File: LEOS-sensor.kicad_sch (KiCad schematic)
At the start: 23 parts, among them J1 MicroFit_1x4, J2 MicroFit_1x4, U1 MCP2562FD, U2 MCP2518FD, Y1 40 MHz

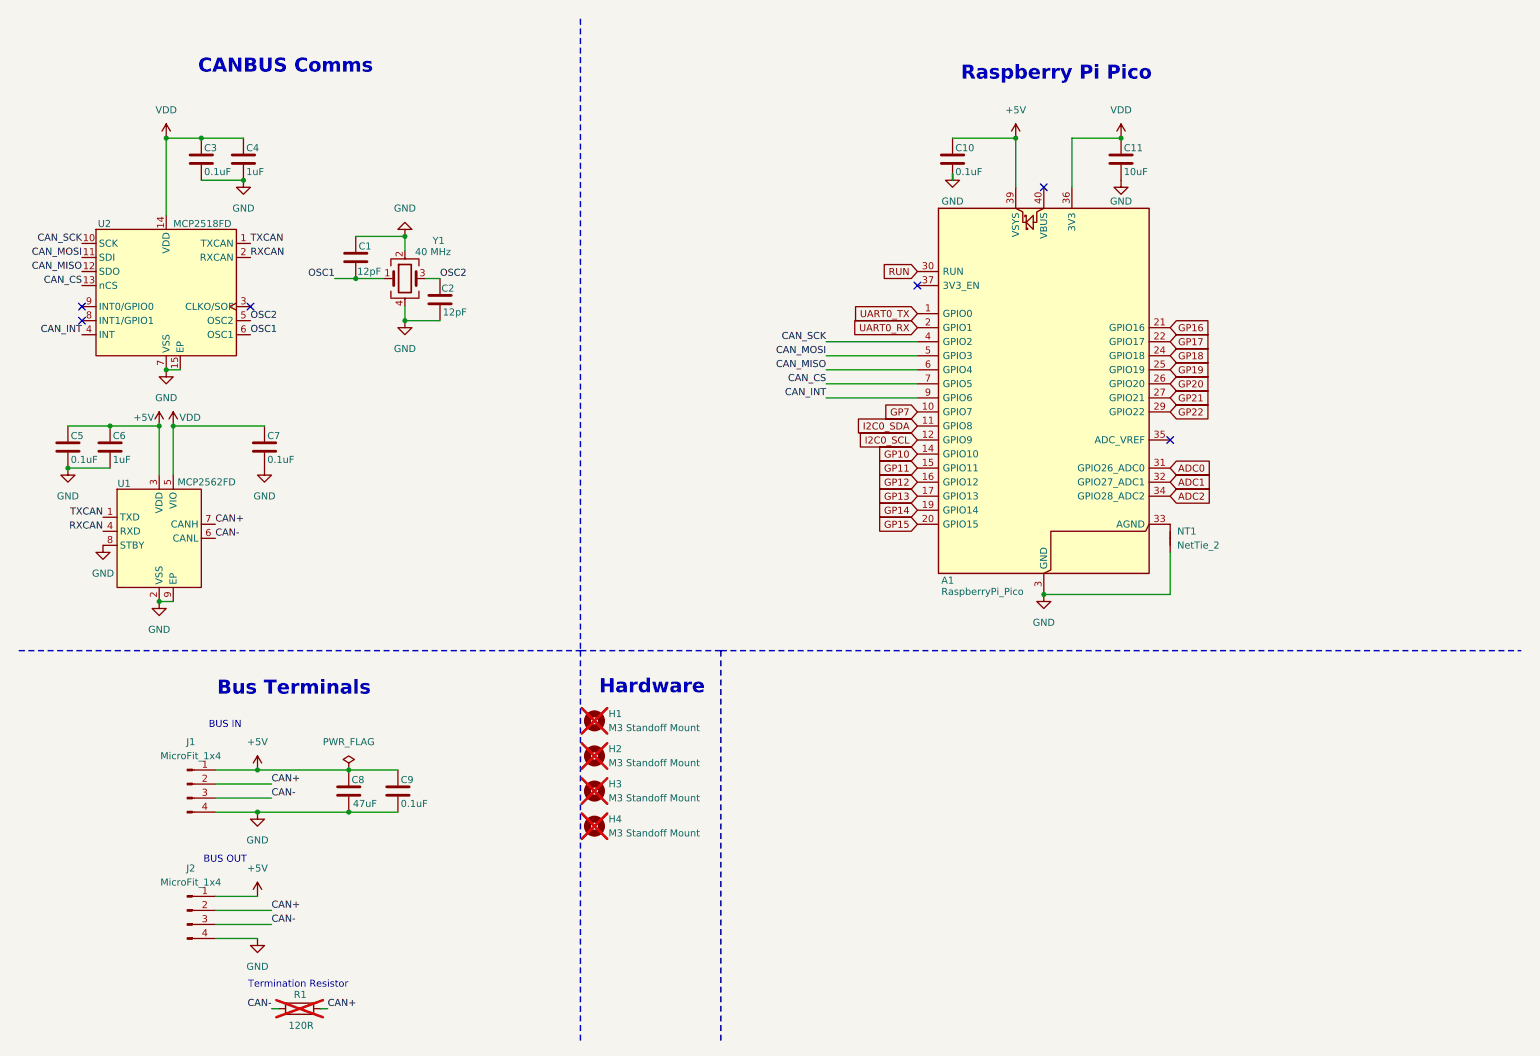
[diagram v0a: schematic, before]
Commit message: Routed and schematiced sensor board
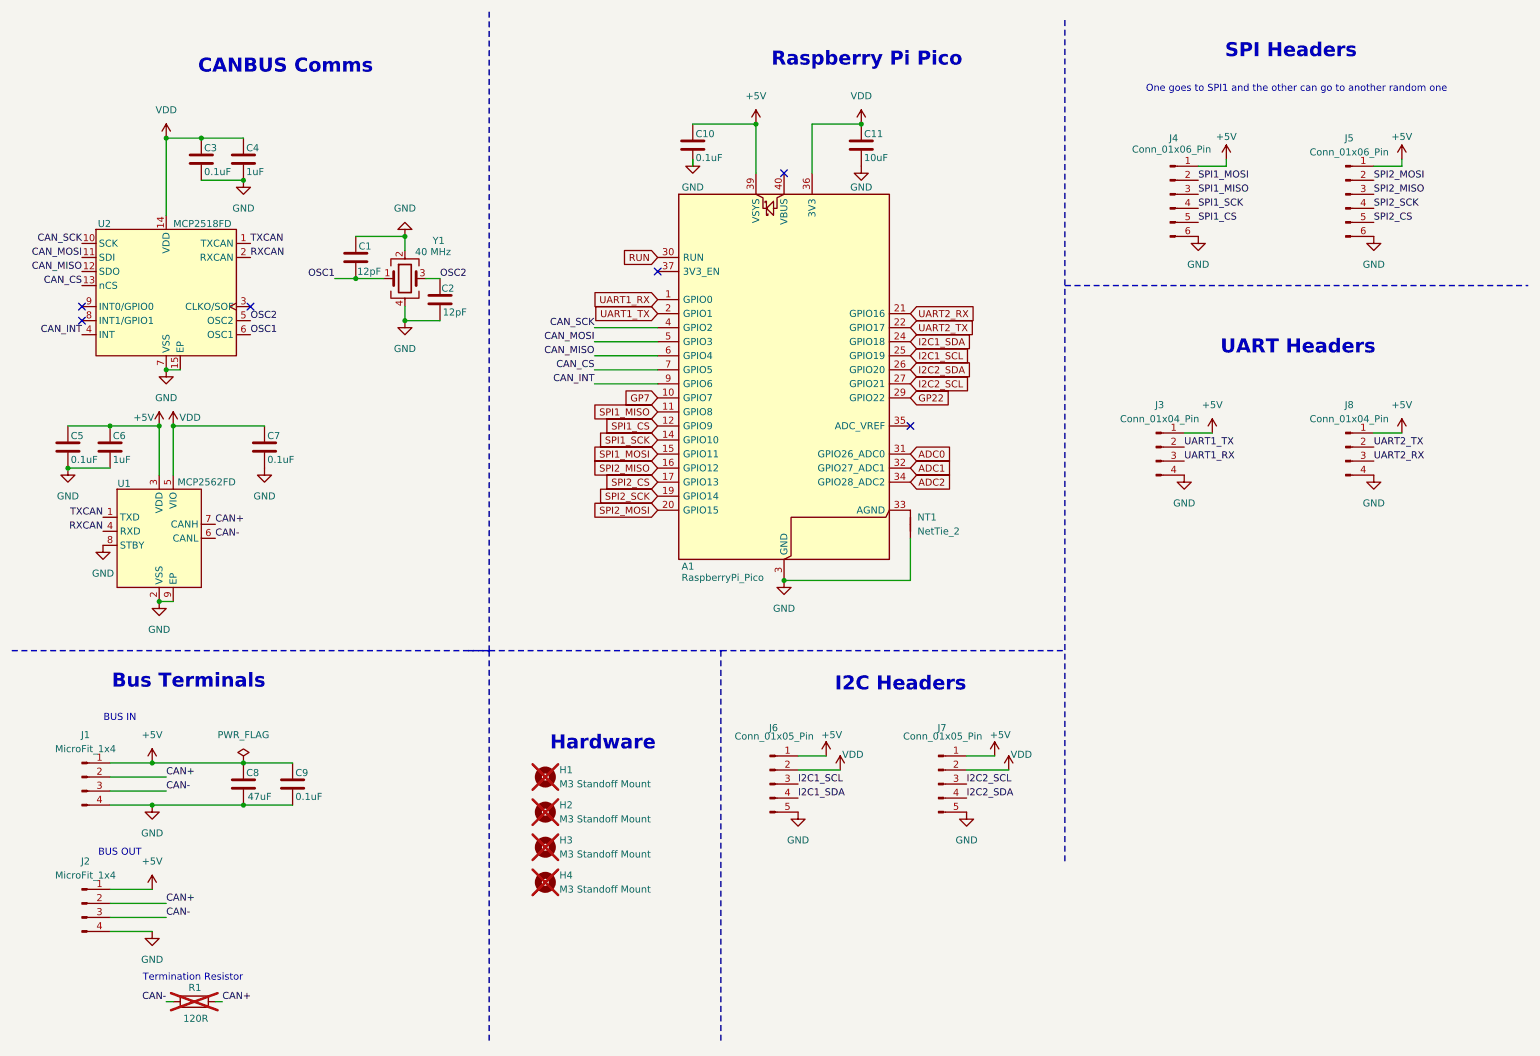
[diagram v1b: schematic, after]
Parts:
- added J3, J8: Conn_01x04_Pin, Connector_PinSocket_2.54mm:PinSocket_1x04_P2.54mm_Horizontal, symbol Connector:Conn_01x04_Pin
- added J4, J5: Conn_01x06_Pin, Connector_PinSocket_2.54mm:PinSocket_1x06_P2.54mm_Horizontal, symbol Connector:Conn_01x06_Pin
- added J6, J7: Conn_01x05_Pin, Connector_PinSocket_2.54mm:PinSocket_1x05_P2.54mm_Horizontal, symbol Connector:Conn_01x05_Pin
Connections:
- net +5V: now also J3.1 (Pin_1), J4.1 (Pin_1), J5.1 (Pin_1), J6.1 (Pin_1), J7.1 (Pin_1), J8.1 (Pin_1)
- net GND: now also J3.4 (Pin_4), J4.6 (Pin_6), J5.6 (Pin_6), J6.5 (Pin_5), J7.5 (Pin_5), J8.4 (Pin_4)
- net VDD: now also J6.2 (Pin_2), J7.2 (Pin_2)
- net GP10 renamed SPI1_SCK
- net SPI1_SCK: now also J4.4 (Pin_4)
- net GP11 renamed SPI1_MOSI
- net SPI1_MOSI: now also J4.2 (Pin_2)
- net GP12 renamed SPI2_MISO
- net SPI2_MISO: now also J5.3 (Pin_3)
- net GP13 renamed SPI2_CS
- net SPI2_CS: now also J5.5 (Pin_5)
- net GP14 renamed SPI2_SCK
- net SPI2_SCK: now also J5.4 (Pin_4)
- net GP15 renamed SPI2_MOSI
- net SPI2_MOSI: now also J5.2 (Pin_2)
- net GP16 renamed UART2_RX
- net UART2_RX: now also J8.3 (Pin_3)
- net GP17 renamed UART2_TX
- net UART2_TX: now also J8.2 (Pin_2)
- net GP18 renamed I2C1_SDA
- net I2C1_SDA: now also J6.4 (Pin_4)
- net GP19 renamed I2C1_SCL
- net I2C1_SCL: now also J6.3 (Pin_3)
- net GP20 renamed I2C2_SDA
- net I2C2_SDA: now also J7.4 (Pin_4)
- net GP21 renamed I2C2_SCL
- net I2C2_SCL: now also J7.3 (Pin_3)
- net I2C0_SCL renamed SPI1_CS
- net SPI1_CS: now also J4.5 (Pin_5)
- net I2C0_SDA renamed SPI1_MISO
- net SPI1_MISO: now also J4.3 (Pin_3)
- net UART0_RX renamed UART1_TX
- net UART1_TX: now also J3.2 (Pin_2)
- net UART0_TX renamed UART1_RX
- net UART1_RX: now also J3.3 (Pin_3)
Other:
- note added: "I2C Headers"
- note added: "One goes to SPI1 and the other can go to another random one"
- note added: "SPI Headers"
- note added: "UART Headers"
- moved on the sheet: A1, C10, C11, C8, C9, H1, H2, H3, H4, J1, J2, NT1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

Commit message: Converted schematic to Socket schematics and routed all headers
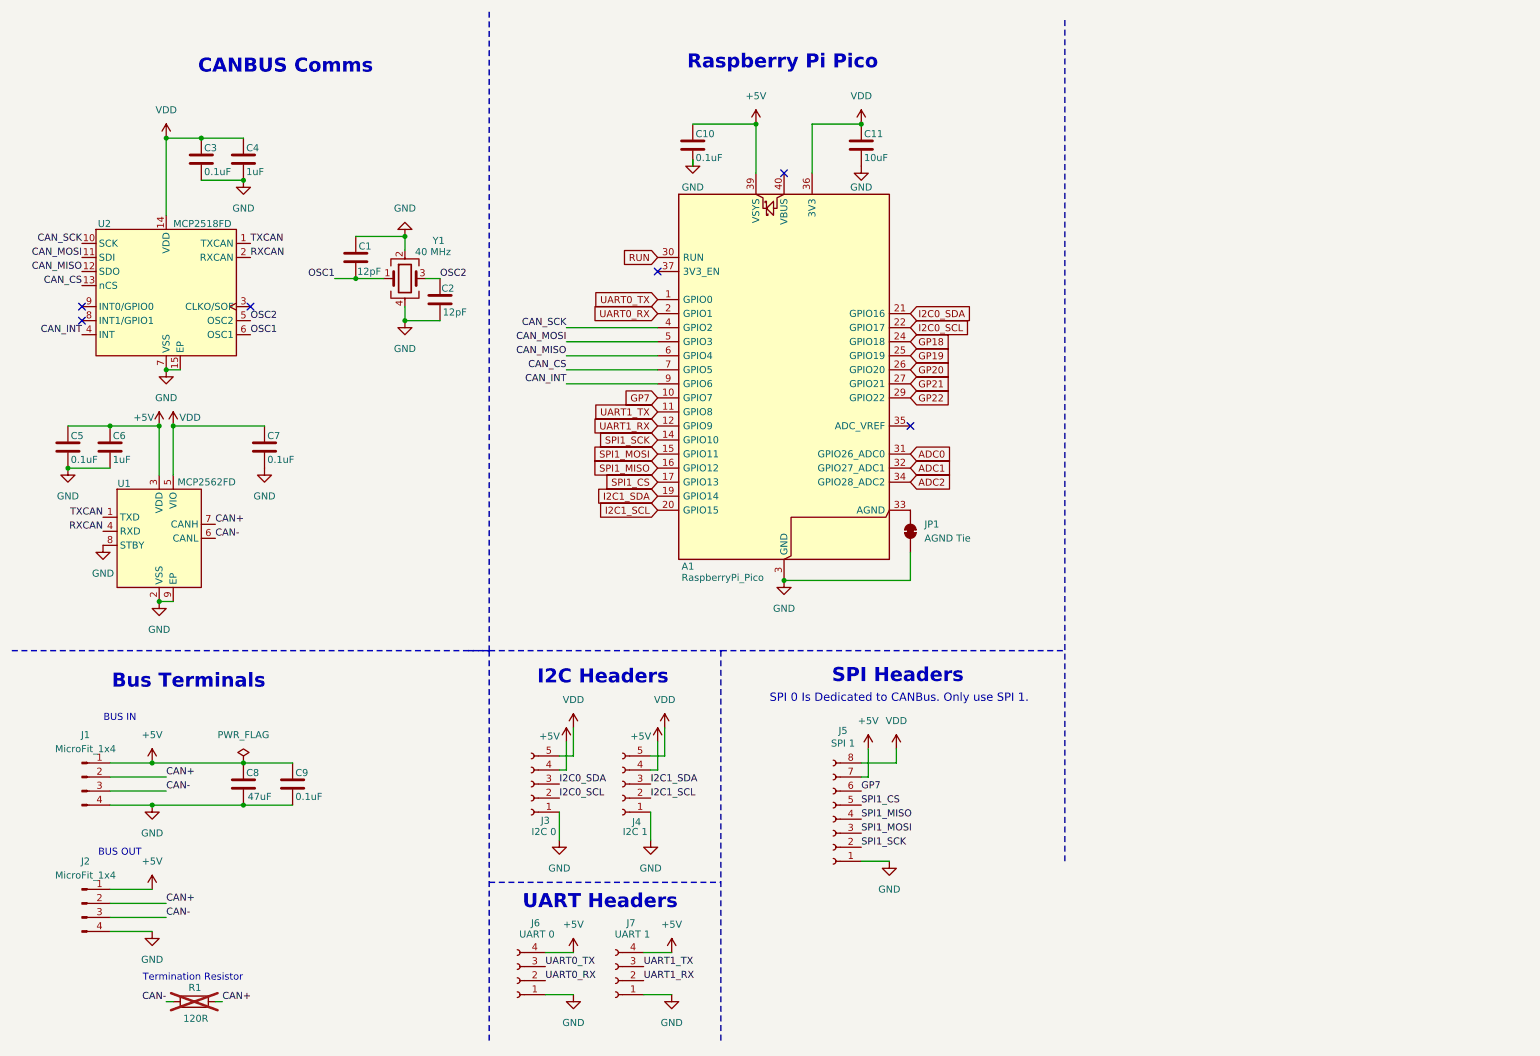
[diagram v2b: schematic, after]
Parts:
- removed H1, H2, H3, H4: M3 Standoff Mount, MountingHole:MountingHole_3.2mm_M3, symbol Mechanical:MountingHole
- removed J4, J5: Conn_01x06_Pin, Connector_PinSocket_2.54mm:PinSocket_1x06_P2.54mm_Horizontal, symbol Connector:Conn_01x06_Pin
- removed J7: Conn_01x05_Pin, Connector_PinSocket_2.54mm:PinSocket_1x05_P2.54mm_Horizontal, symbol Connector:Conn_01x05_Pin
- removed J8: Conn_01x04_Pin, Connector_PinSocket_2.54mm:PinSocket_1x04_P2.54mm_Horizontal, symbol Connector:Conn_01x04_Pin
- removed NT1: NetTie_2, Jumper:SolderJumper-2_P1.3mm_Bridged_RoundedPad1.0x1.5mm, symbol Device:NetTie_2
- added J3: I2C 0, Connector_PinSocket_2.54mm:PinSocket_1x05_P2.54mm_Horizontal, symbol Connector:Conn_01x05_Socket
- added J5: SPI 1, Connector_PinSocket_2.54mm:PinSocket_1x08_P2.54mm_Horizontal, symbol Connector:Conn_01x08_Socket
- added J7: UART 1, Connector_PinSocket_2.54mm:PinSocket_1x04_P2.54mm_Horizontal, symbol Connector:Conn_01x04_Socket
- added JP1: AGND Tie, Jumper:SolderJumper-2_P1.3mm_Bridged_RoundedPad1.0x1.5mm, symbol Jumper:SolderJumper_2_Bridged
- C1, C10, C11, C2, C3, C4, C5, C6, C7, C8, C9: footprint Capacitor_SMD:C_0201_0603Metric -> Capacitor_SMD:C_0603_1608Metric
- J4: renamed from J6; value Conn_01x05_Pin -> I2C 1; symbol Connector:Conn_01x05_Pin -> Connector:Conn_01x05_Socket
- J6: renamed from J3; value Conn_01x04_Pin -> UART 0; symbol Connector:Conn_01x04_Pin -> Connector:Conn_01x04_Socket
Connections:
- net SPI2_CS is gone; now on net SPI1_CS: A1.17 (GPIO13)
- net SPI2_MISO is gone; now on net SPI1_MISO: A1.16 (GPIO12)
- net SPI2_MOSI is gone; now on net I2C1_SCL: A1.20 (GPIO15)
- net SPI2_SCK is gone; now on net I2C1_SDA: A1.19 (GPIO14)
- net +5V: now also J4.4 (Pin_4), J6.4 (Pin_4), J3.4 (Pin_4), J5.7 (Pin_7), J7.4 (Pin_4); no longer J4.1 (Pin_1), J6.1 (Pin_1)
- net GND: now also J4.1 (Pin_1), J6.1 (Pin_1), J3.1 (Pin_1), J5.1 (Pin_1), J7.1 (Pin_1), JP1.1 (A); no longer J4.5 (Pin_5), J6.4 (Pin_4)
- net GP7: now also J5.6 (Pin_6)
- net I2C1_SCL: now also J4.2 (Pin_2); no longer A1.25 (GPIO19), J4.3 (Pin_3)
- net I2C1_SDA: now also J4.3 (Pin_3); no longer A1.24 (GPIO18), J4.4 (Pin_4)
- net SPI1_CS: now also J5.5 (Pin_5); no longer A1.12 (GPIO9)
- net SPI1_MISO: now also J5.4 (Pin_4); no longer A1.11 (GPIO8)
- net SPI1_MOSI: now also J5.3 (Pin_3)
- net SPI1_SCK: now also J5.2 (Pin_2)
- net UART1_RX: now also A1.12 (GPIO9), J7.2 (Pin_2); no longer A1.1 (GPIO0), J6.3 (Pin_3)
- net UART1_TX: now also A1.11 (GPIO8), J7.3 (Pin_3); no longer A1.2 (GPIO1), J6.2 (Pin_2)
- net VDD: now also J4.5 (Pin_5), J3.5 (Pin_5), J5.8 (Pin_8); no longer J4.2 (Pin_2)
- net at A1.33 (AGND): now also JP1.2 (B)
- net I2C2_SCL renamed GP21
- net I2C2_SDA renamed GP20
- net UART2_RX renamed I2C0_SDA
- net I2C0_SDA: now also J3.3 (Pin_3)
- net UART2_TX renamed I2C0_SCL
- net I2C0_SCL: now also J3.2 (Pin_2)
- new net GP18: A1.24 (GPIO18)
- new net GP19: A1.25 (GPIO19)
- new net UART0_RX: A1.2 (GPIO1), J6.2 (Pin_2)
- new net UART0_TX: A1.1 (GPIO0), J6.3 (Pin_3)
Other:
- note added: "SPI 0 Is Dedicated to CANBus. Only use SPI 1."
- note removed: "Hardware"
- note removed: "One goes to SPI1 and the other can go to another random one"
